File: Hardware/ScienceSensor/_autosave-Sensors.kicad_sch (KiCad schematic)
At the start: 10 parts

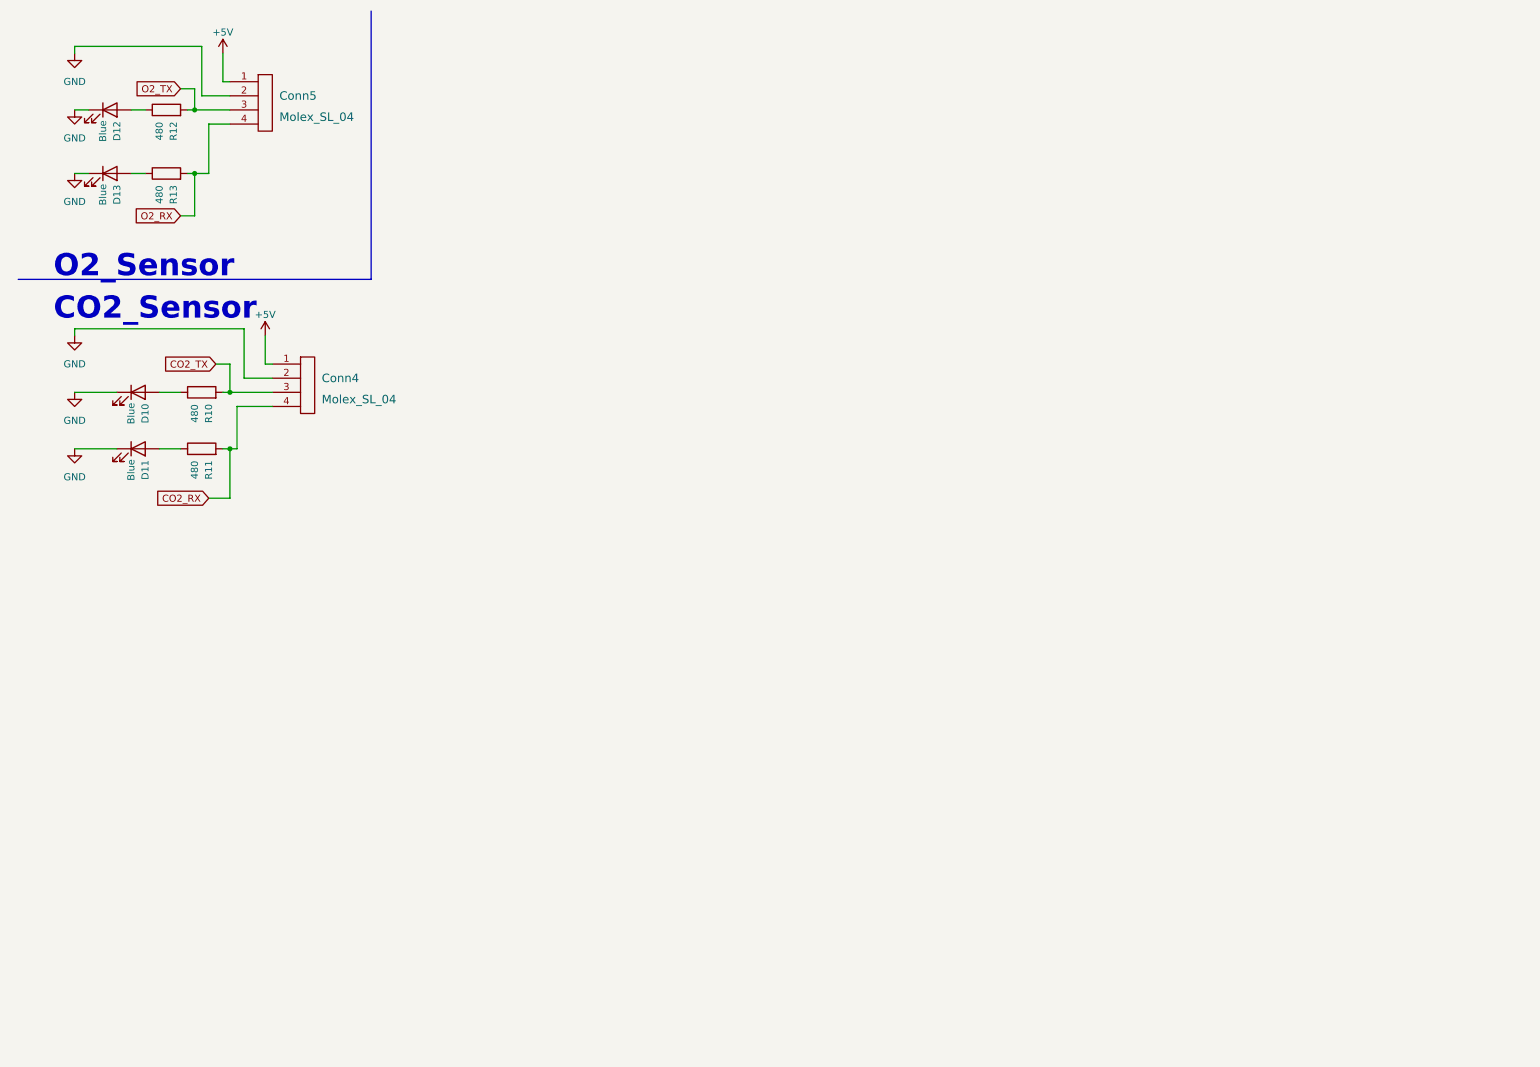
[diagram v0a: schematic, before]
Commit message: Created NO sensor, NH3 sensor, worked on Mosfets, and created Methane sensor with labels.
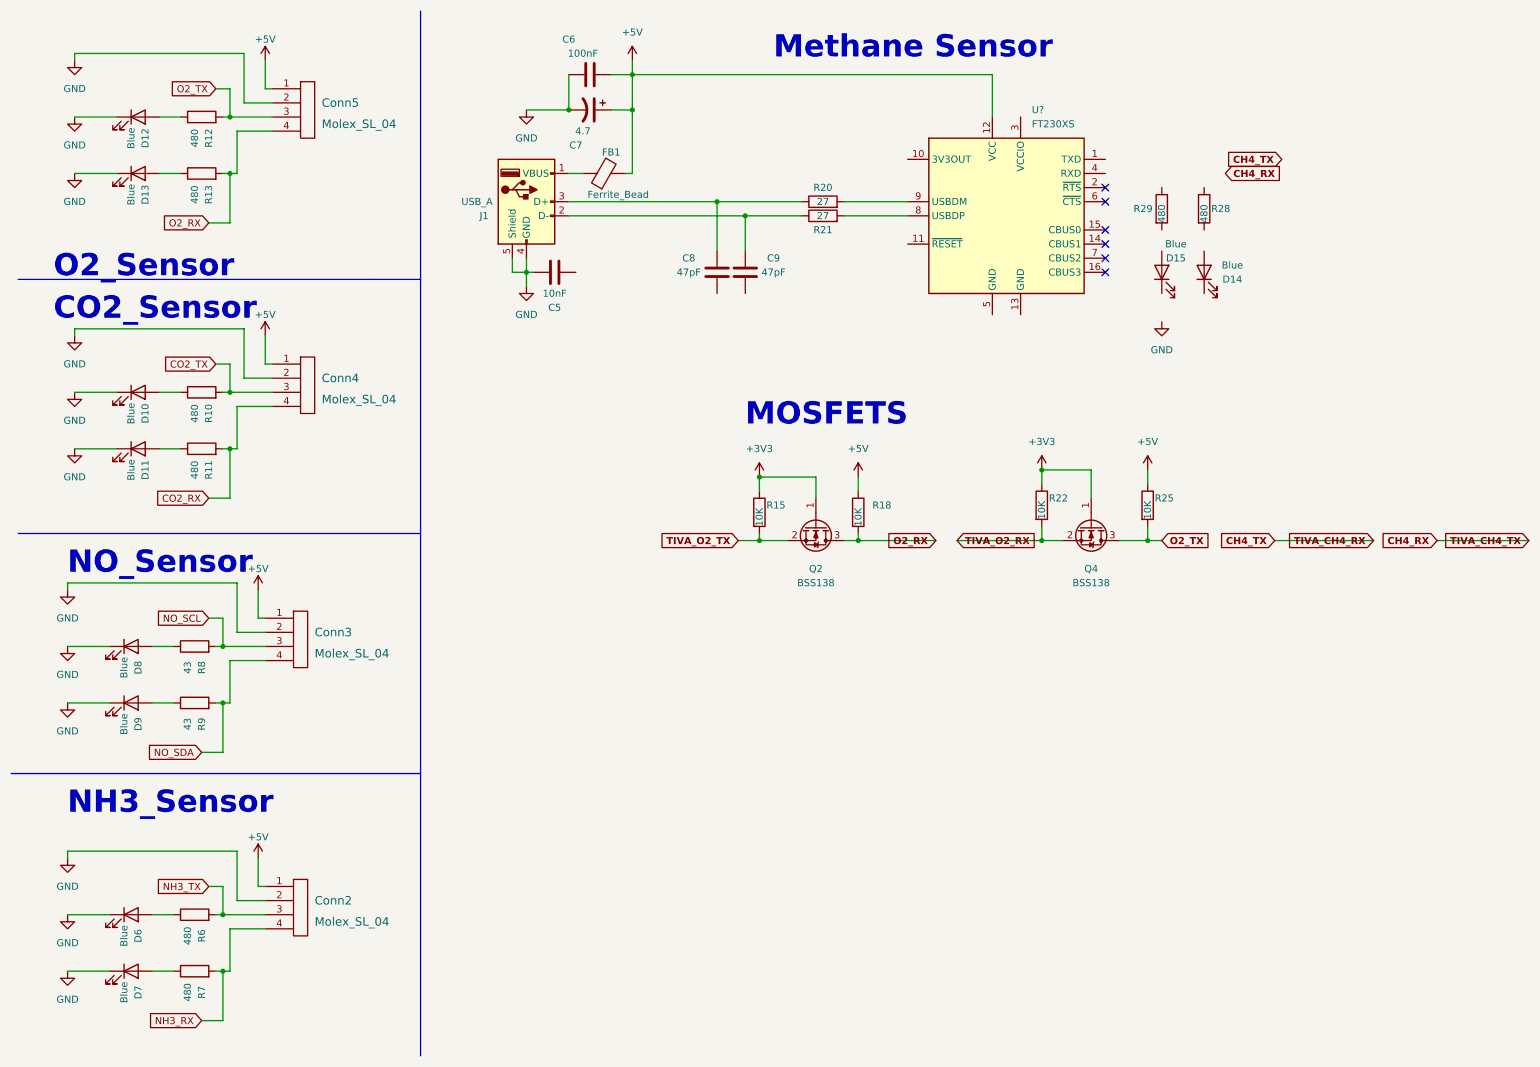
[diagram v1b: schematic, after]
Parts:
- removed Blue: D13, symbol Device:LED
- removed Blue: D12, symbol Device:LED
- added Blue: D9, symbol Device:LED
- added Blue: D14, symbol Device:LED
- added Blue: D6, symbol Device:LED
- added Blue: D8, symbol Device:LED
- added Blue: D12, symbol Device:LED
- added Blue: D13, symbol Device:LED
- added Blue: D15, symbol Device:LED
- added Blue: D7, symbol Device:LED
- added C5: 10nF, symbol Device:C
- added C6: 100nF, symbol Device:C
- added C7: 4.7, symbol Device:C_Polarized_US
- added C8, C9: 47pF, symbol Device:C
- added Conn2, Conn3: Molex_SL_04, symbol MRDT_Connectors:Molex_SL_04
- added FB1: Ferrite_Bead, symbol Device:FerriteBead
- added J1: USB_A, symbol Connector:USB_A
- added Q2, Q4: BSS138, symbol Device:Q_NMOS_GSD
- added R15, R18, R22, R25: 10K, symbol Device:R
- added R20, R21: 27, symbol Device:R
- added R28, R29, R6, R7: 480, symbol Device:R
- added R8, R9: 43, symbol Device:R
- added U?: FT230XS, Package_SO:SSOP-16_3.9x4.9mm_P0.635mm, symbol Interface_USB:FT230XS
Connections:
- net +5V: now also C6.2, C7.1, Conn2.1, Conn3.1, FB1.2, R18.1, R25.1, U?.12 (VCC)
- net GND: now also Blue.1 (K), Blue.1 (K), Blue.1 (K), Blue.1 (K), Blue.1 (K), Blue.1 (K), C5.1, C6.1, C7.2, Conn2.2, Conn3.2, J1.4 (GND), J1.5 (Shield)
- net O2_RX: now also Q2.3 (D), R18.2
- net O2_TX: now also Q4.3 (D), R25.2
- net at R13.1: now also Blue.2 (A)
- net at R12.1: now also Blue.2 (A)
- new net: Blue.2 (A), R7.1
- new net: FB1.1, J1.1 (VBUS)
- new net: C9.2, J1.2 (D-), R21.1
- new net: C8.2, J1.3 (D+), R20.1
- new net: Blue.2 (A), R9.1
- new net: R20.2, U?.9 (USBDM)
- new net: Blue.2 (A), R8.1
- new net: Blue.2 (A), R6.1
- new net: R21.2, U?.8 (USBDP)
- new net +3V3: Q2.1 (G), Q4.1 (G), R15.1, R22.1
- new net NH3_RX: Conn2.4, R7.2
- new net NH3_TX: Conn2.3, R6.2
- new net NO_SCL: Conn3.3, R8.2
- new net NO_SDA: Conn3.4, R9.2
- new net TIVA_O2_RX: Q4.2 (S), R22.2
- new net TIVA_O2_TX: Q2.2 (S), R15.2
- no-connect marks 0 -> 6
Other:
- note added: "MOSFETS"
- note added: "Methane Sensor"
- note added: "NH3_Sensor"
- note added: "NO_Sensor"
